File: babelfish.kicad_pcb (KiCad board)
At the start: 2 copper layers, 56 x 38.2 mm, 65 parts, among them J1 Conn_02x02_Odd_Even, J3 SWD, J5 IO_A, J7 USB_A, Q1 BSS138, SW1 K2-1836UQ-C3DW-06, U1 RP2040, U2 W25Q128JVS, U3 AMS1117-3.3, U4 GT-USB-7010ASV, X1 X322512MSB4SI

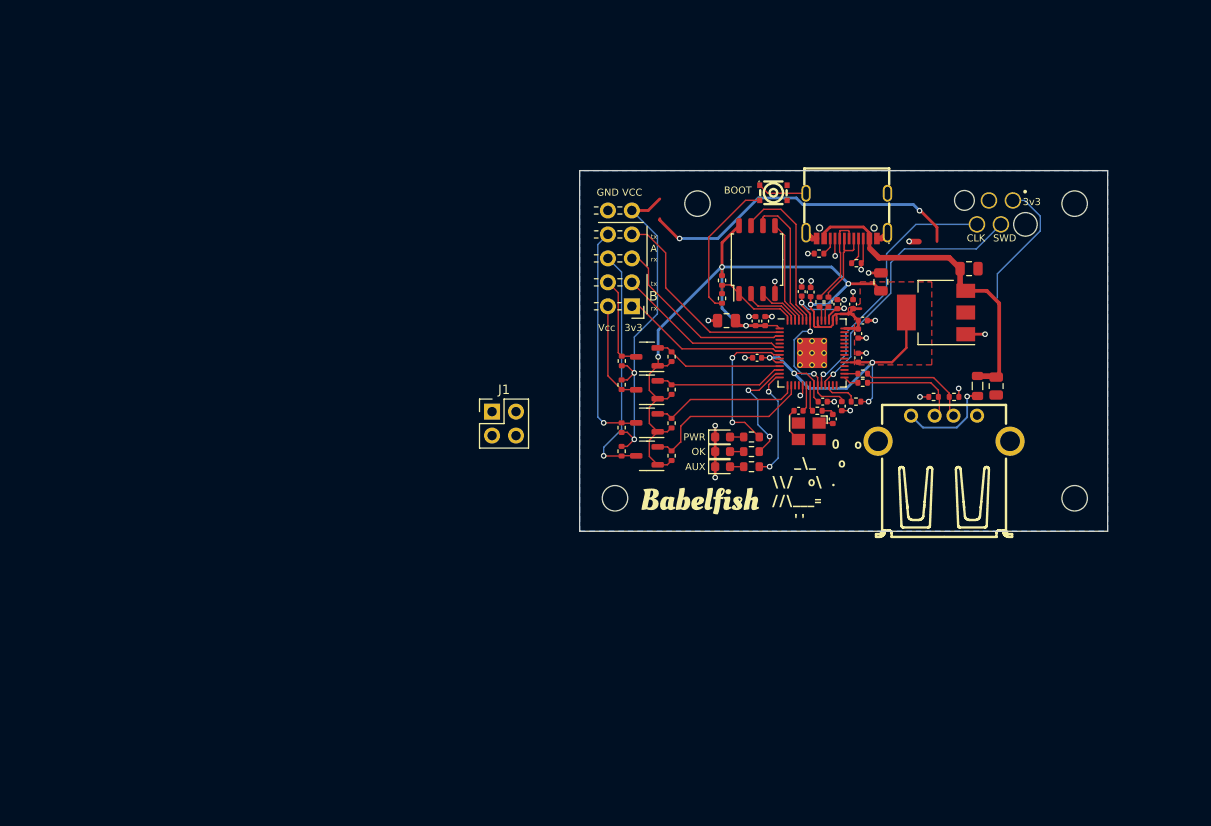
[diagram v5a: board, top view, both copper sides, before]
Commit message: Added muxes
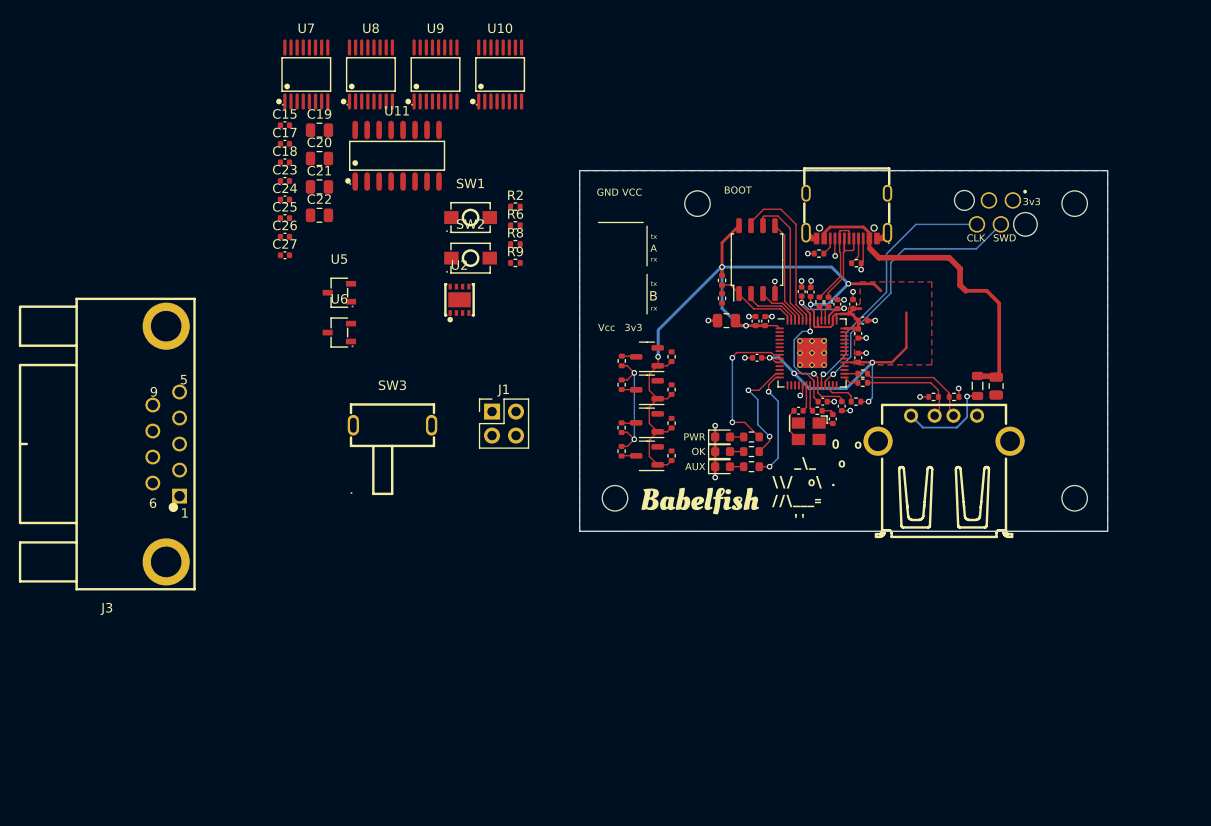
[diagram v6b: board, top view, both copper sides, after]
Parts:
- removed the C1 at (123.5, 79.9)
- removed the C4 at (114.2, 81.3)
- removed J5: IO_A, Connector_PinHeader_2.54mm:PinHeader_2x05_P2.54mm_Horizontal
- removed the U3 at (120.0, 84.5)
- added C15: 100n, Capacitor_SMD:C_0402_1005Metric, F.Cu at (51.0, 64.7)
- added C17: 1u, Capacitor_SMD:C_0402_1005Metric, F.Cu at (51.0, 66.7)
- added C18: 100n, Capacitor_SMD:C_0402_1005Metric, F.Cu at (51.0, 68.6)
- added C19: 10u, Capacitor_SMD:C_0805_2012Metric, F.Cu at (54.7, 65.2)
- added C20: 10u, Capacitor_SMD:C_0805_2012Metric, F.Cu at (54.7, 68.2)
- added C21: 10u, Capacitor_SMD:C_0805_2012Metric, F.Cu at (54.7, 71.2)
- added C22: 10u, Capacitor_SMD:C_0805_2012Metric, F.Cu at (54.7, 74.2)
- added C23: 100n, Capacitor_SMD:C_0402_1005Metric, F.Cu at (51.0, 70.6)
- added C24: 100n, Capacitor_SMD:C_0402_1005Metric, F.Cu at (51.0, 72.6)
- added C25: 100n, Capacitor_SMD:C_0402_1005Metric, F.Cu at (51.0, 74.5)
- added C26: 100n, Capacitor_SMD:C_0402_1005Metric, F.Cu at (51.0, 76.5)
- added C27: 100n, Capacitor_SMD:C_0402_1005Metric, F.Cu at (51.0, 78.5)
- added J3: DE9 Female, lcsc:DSUB-TH_DMR-9S, F.Cu at (38.4, 98.5)
- added R2: 10k, Resistor_SMD:R_0402_1005Metric, F.Cu at (75.4, 73.3)
- added R6: 10k2, Resistor_SMD:R_0402_1005Metric, F.Cu at (75.4, 75.3)
- added R8: 2k05, Resistor_SMD:R_0402_1005Metric, F.Cu at (75.4, 77.3)
- added R9: 1k4, Resistor_SMD:R_0402_1005Metric, F.Cu at (75.4, 79.3)
- added SW2: TS342A2P-WZ, lcsc:SW-SMD_L4.0-W2.9-LS5.0, F.Cu at (70.7, 78.8)
- added SW3: SK12D07VG5_C3020419, lcsc:SW-TH_SHOU_SK12D07VG5, F.Cu at (62.4, 96.5)
- added U10: 74HC4052PW,118, lcsc:TSSOP-16_L5.0-W4.4-P0.65-LS6.4-BL, F.Cu at (73.8, 59.3)
- added U11: MAX3232IDR, lcsc:SOIC-16_L9.9-W3.9-P1.27-LS6.0-BL, F.Cu at (62.9, 67.9)
- added U2: TPS2113ADRBR, lcsc:SON-8_L3.0-W3.0-P0.65-LS3.0-BL-EP, F.Cu at (69.5, 83.2)
- added U5: TPMCP1703T-5002E_CB, lcsc:SOT-23-3_L2.9-W1.6-P1.90-LS2.8-BR, F.Cu at (56.8, 82.4)
- added U6: TPMCP1703T-3302E_CB, lcsc:SOT-23-3_L2.9-W1.6-P1.90-LS2.8-BR, F.Cu at (56.8, 86.7)
- added U7: 74HC4052PW,118, lcsc:TSSOP-16_L5.0-W4.4-P0.65-LS6.4-BL, F.Cu at (53.3, 59.3)
- added U8: 74HC4052PW,118, lcsc:TSSOP-16_L5.0-W4.4-P0.65-LS6.4-BL, F.Cu at (60.1, 59.3)
- added U9: 74HC4052PW,118, lcsc:TSSOP-16_L5.0-W4.4-P0.65-LS6.4-BL, F.Cu at (67.0, 59.3)
- SW1: value K2-1836UQ-C3DW-06 -> TS342A2P-WZ; footprint lcsc:SW-SMD_4P-L2.8-W2.4-P1.60-LS3.0 -> lcsc:SW-SMD_L4.0-W2.9-LS5.0
- moved SW1 32.2 mm to (70.7, 74.5)
- renumbered C6 to C1, C16 to C10, C2 to C11, C3 to C12, C8 to C13, C10 to C14, C5 to C16, C7 to C2, C22 to C28, C17 to C3, C9 to C4, C11 to C5, C12 to C6, C13 to C7, C14 to C8, C15 to C9, D2 to D1, D4 to D2, D5 to D3, J3 to J2, J7 to J4, R20 to R1, R6 to R10, R1 to R11, R5 to R12, R11 to R13, R8 to R14, R21 to R15, R22 to R16, R23 to R17, R12 to R18, R13 to R19, R14 to R20, R15 to R21, R16 to R22, R17 to R23, R18 to R24, R19 to R25, R10 to R26, R9 to R27, R7 to R5, R2 to R7, U4 to U3, U2 to U4
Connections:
- net /U0_RX_C renamed /GPIO17
- net /U0_RX_CH renamed /RX_A_2Y1
- net /U0_TX_C renamed /GPIO16
- net /U0_TX_CH renamed /TX_A_2Y1
- net /U1_RX_C renamed /GPIO21
- net /U1_TX_C renamed /GPIO20
- net /VSH renamed /VSHIFT
- J1 pad 1: VBUS -> /5V0
- Q1 pad 2: /U0_TX_B -> /TX_A_1Y1
- Q2 pad 2: /U0_RX_B -> /RX_A_1Y1
- Q3 pad 2: /U1_TX_B -> /TX_B_1Y1
- Q3 pad 3: /U1_TX_CH -> /RX_B_2Y1
- Q4 pad 2: /U1_RX_B -> /RX_B_1Y1
- Q4 pad 3: /U1_RX_CH -> /RX_B_2Y1
- R18 pad 2: /U0_TX_B -> /TX_A_1Y1
- R20 pad 2: /U0_RX_B -> /RX_A_1Y1
- R22 pad 2: /U1_TX_B -> /TX_B_1Y1
- R23 pad 2: /U1_TX_CH -> /RX_B_2Y1
- R24 pad 2: /U1_RX_B -> /RX_B_1Y1
- R25 pad 2: /U1_RX_CH -> /RX_B_2Y1
- U1 pad 11: /U1_TX_B -> /TX_B
- U1 pad 12: /U1_RX_B -> /RX_B
- U1 pad 2: /U0_TX_A -> /TX_A
- U1 pad 3: /U0_RX_A -> /RX_A
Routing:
- net /VCC_IN: track 36.5 -> 0.00 mm, vias 2 -> 0
- net VBUS: track 69.6 -> 34.6 mm, vias 2 -> 0
- net /RX_A_2Y1: track 25.8 -> 1.52 mm, vias 1 -> 0
- net /TX_A_2Y1: track 24.1 -> 1.55 mm, vias 1 -> 0
- net /U0_TX_A: track 22.1 -> 0.00 mm
- net /U0_RX_A: track 20.2 -> 0.00 mm
- net /U0_RX_B: track 18.8 -> 0.00 mm
- net /U1_TX_A: track 18.5 -> 0.00 mm
- net /U1_RX_A: track 17.6 -> 0.00 mm
- net /U0_TX_B: track 15.9 -> 0.00 mm
- net /~{USB_BOOT}: track 15.0 -> 0.00 mm
- net +3V3: track 139.9 -> 125.6 mm
- net /U1_RX_B: track 13.8 -> 0.00 mm
- net /U1_TX_B: track 13.7 -> 0.00 mm
- net /VSHIFT: track 0.00 -> 13.7 mm, vias 0 -> 2
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
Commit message: Layout v2 done
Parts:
- removed FB1: FerriteBead_Small, Inductor_SMD:L_0805_2012Metric
- added C29: 10u, Capacitor_SMD:C_0805_2012Metric, F.Cu at (121.6, 99.2)
- added C30: 100n, Capacitor_SMD:C_0402_1005Metric, F.Cu at (123.9, 96.1)
- added C31: 10u, Capacitor_SMD:C_0805_2012Metric, F.Cu at (121.6, 95.8)
- added R28: 10k, Resistor_SMD:R_0402_1005Metric, F.Cu at (126.4, 100.8)
- added U12: AP2191WG-7, lcsc:SOT-25-5_L2.9-W1.6-P0.95-LS2.8-BL, F.Cu at (124.4, 98.9)
- C28: value 10u -> 100n; footprint Capacitor_SMD:C_0805_2012Metric -> Capacitor_SMD:C_0402_1005Metric
- J1: value Conn_02x02_Odd_Even -> Shifter Power; footprint Connector_PinHeader_2.54mm:PinHeader_2x02_P2.54mm_Vertical -> Connector_PinHeader_2.54mm:PinHeader_1x03_P2.54mm_Vertical
- moved J3 93.4 mm to (131.6, 92.1), turned to 0 degrees
- moved C18 76.0 mm to (125.8, 82.1)
- moved C17 74.5 mm to (123.9, 82.1), turned to 180 degrees
- moved C15 74.1 mm to (122.7, 83.5), turned to -90 degrees
- moved C19 73.9 mm to (127.4, 78.2), turned to -90 degrees
- moved SW3 68.6 mm to (127.0, 73.5), turned to 180 degrees
- moved U5 67.7 mm to (124.3, 78.2), turned to 180 degrees
- moved C20 67.6 mm to (121.3, 79.5), turned to -90 degrees
- moved C22 66.9 mm to (120.3, 86.9)
- moved C27 64.2 mm to (106.0, 111.5), turned to -90 degrees
- moved C21 63.9 mm to (117.8, 81.5), turned to 180 degrees
- moved C26 63.6 mm to (104.4, 111.0)
- moved U6 63.3 mm to (120.0, 83.6), turned to -90 degrees
- moved C24 62.7 mm to (100.5, 111.0)
- moved C23 59.9 mm to (98.7, 106.8), turned to -90 degrees
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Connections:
- net Net-(U2-VSNS) renamed /PWR_VSNS
- C28 pad 1: VBUS -> /VBUS_OUT
- J1 pad 1: /5V0 -> /VCC_IN
- J1 pad 3: /VCC_IN -> /5V0
- J3 pad 2: /RX_A_CONN -> /TX_A_CONN
- J3 pad 3: /TX_A_CONN -> /TX_B_CONN
- J3 pad 4: unconnected-(J3-Pad4) -> /GPIO14
- J3 pad 5: unconnected-(J3-Pad5) -> /GPIO13
- J3 pad 7: /RX_B_CONN -> /RX_A_CONN
- J3 pad 8: /TX_B_CONN -> /RX_B_CONN
- J3 pad 9: unconnected-(J3-Pad9) -> /GPIO12
- J4 pad 1: Net-(J4-VBUS) -> /VBUS_OUT
- Q1 pad 2: /TX_A_1Y1 -> /RX_A_1Y1
- Q1 pad 3: /TX_A_2Y1 -> /RX_A_2Y1
- Q2 pad 2: /RX_A_1Y1 -> /TX_A_1Y1
- Q2 pad 3: /RX_A_2Y1 -> /TX_A_2Y1
- Q3 pad 3: /RX_B_2Y1 -> /TX_B_2Y1
- R18 pad 2: /TX_A_1Y1 -> /RX_A_1Y1
- R19 pad 2: /TX_A_2Y1 -> /RX_A_2Y1
- R20 pad 2: /RX_A_1Y1 -> /TX_A_1Y1
- R21 pad 2: /RX_A_2Y1 -> /TX_A_2Y1
- R23 pad 2: /RX_B_2Y1 -> /TX_B_2Y1
- U1 pad 15: /U0_TX_B -> /GPIO12
- U1 pad 16: /U0_RX_B -> /GPIO13
- U1 pad 31: /GPIO20 -> /USB2_EN
- U1 pad 32: /GPIO21 -> /USB2_FLG
- U1 pad 35: /GPIO23 -> /STAT_5V0
- U1 pad 4: /GPIO2 -> /CH_A_S0
- U1 pad 5: /GPIO3 -> /CH_A_S1
- U10 pad 1: /RX_B_2Y0 -> /RX_B_Y0_THRU
- U10 pad 12: /RX_B_1Y0 -> /RX_B_Y0_THRU
- U10 pad 13: /RX_A -> /RX_B
- U11 pad 7: /RX_B_1Y2 -> /TX_B_2Y2
- U11 pad 8: /TX_B_2Y2 -> /RX_B_2Y2
- U7 pad 1: /TX_A_2Y0 -> /TX_A_Y0_THRU
- U7 pad 12: /TX_A_1Y0 -> /TX_A_Y0_THRU
- U8 pad 1: /RX_A_2Y0 -> /RX_A_Y0_THRU
- U8 pad 12: /RX_A_1Y0 -> /RX_A_Y0_THRU
- U9 pad 1: /TX_B_2Y0 -> /TX_B_Y0_THRU
- U9 pad 12: /TX_B_1Y0 -> /TX_B_Y0_THRU
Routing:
- net /VCC_IN: track 0.00 -> 91.3 mm
- net +3V3: track 125.6 -> 62.2 mm, vias 9 -> 21
- net /5V0: track 0.00 -> 59.0 mm, vias 0 -> 6
- net GND: track 42.4 -> 98.8 mm, vias 22 -> 43
- net /RX_B_CONN: track 0.00 -> 49.0 mm, vias 0 -> 1
- net /VSHIFT: track 13.7 -> 60.7 mm, vias 2 -> 4
- net /RX_A_CONN: track 0.00 -> 46.5 mm, vias 0 -> 3
- net /TX_A_CONN: track 0.00 -> 44.0 mm, vias 0 -> 1
- net /TX_B_CONN: track 0.00 -> 42.8 mm, vias 0 -> 1
- net /GPIO12: track 0.00 -> 37.4 mm, vias 0 -> 1
- net /TX_B_2Y2: track 0.00 -> 35.0 mm, vias 0 -> 2
- net /RUN: track 3.67 -> 38.1 mm, vias 0 -> 2
- net /GPIO14: track 0.00 -> 32.9 mm, vias 0 -> 1
- net /GPIO13: track 0.00 -> 32.5 mm, vias 0 -> 1
- net /TX_A_2Y2: track 0.00 -> 28.8 mm, vias 0 -> 2
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- added copper zone on In2.Cu, net +3V3
- added copper zone on In2.Cu, net /5V0
- added copper zone on In1.Cu, net GND
- removed copper zone on B.Cu, net GND
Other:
- board size 56 x 38.2 mm -> 56 x 45.2 mm
- copper layers 2 -> 4
- board text added: "3V3"
- board text added: "RST"
- board text removed: "3v3"
- board text removed: "A"
- board text removed: "B"
- board text removed: "VCC"
- board text removed: "Vcc"
- board text removed: "rx"
- board text removed: "tx"

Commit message: V2 export WIP
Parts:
- added ?: , , F.Cu at (126.5, 93.0)
- added ?: , , F.Cu at (124.8, 92.0)
- added ?: , , F.Cu at (124.8, 90.0)
- added ?: , , F.Cu at (126.5, 89.0)
- added ?: , , F.Cu at (126.5, 91.0)
- moved kibuzzard-644F39EB 67.9 mm to (101.3, 74.3)
- moved kibuzzard-644F3679 47.8 mm to (90.5, 108.5)
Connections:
- J3 pad 9: /GPIO12 -> +3V3
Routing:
- net /GPIO12: track 37.4 -> 0.00 mm, vias 1 -> 0
- net GND: track 98.8 -> 130.4 mm, vias 43 -> 50
- net /5V0: track 59.0 -> 75.5 mm
- net +3V3: track 62.2 -> 75.6 mm, vias 21 -> 22
- net VBUS: track 25.4 -> 34.0 mm
- net /VCC_IN: track 91.3 -> 98.2 mm
- net /STAT_5V0: track 12.0 -> 12.3 mm, vias 0 -> 2
